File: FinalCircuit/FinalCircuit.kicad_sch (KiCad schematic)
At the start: 59 parts, among them J1 Conn_02x20_Odd_Even, J2 Conn_02x06_Odd_Even, J3 Conn_01x06, U1 LM6172, U10 CD4066BE, U11 CD4066BE, U2 OPA2277, U3 MCP3008, U4 MCP4921, U5 CD4066BE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

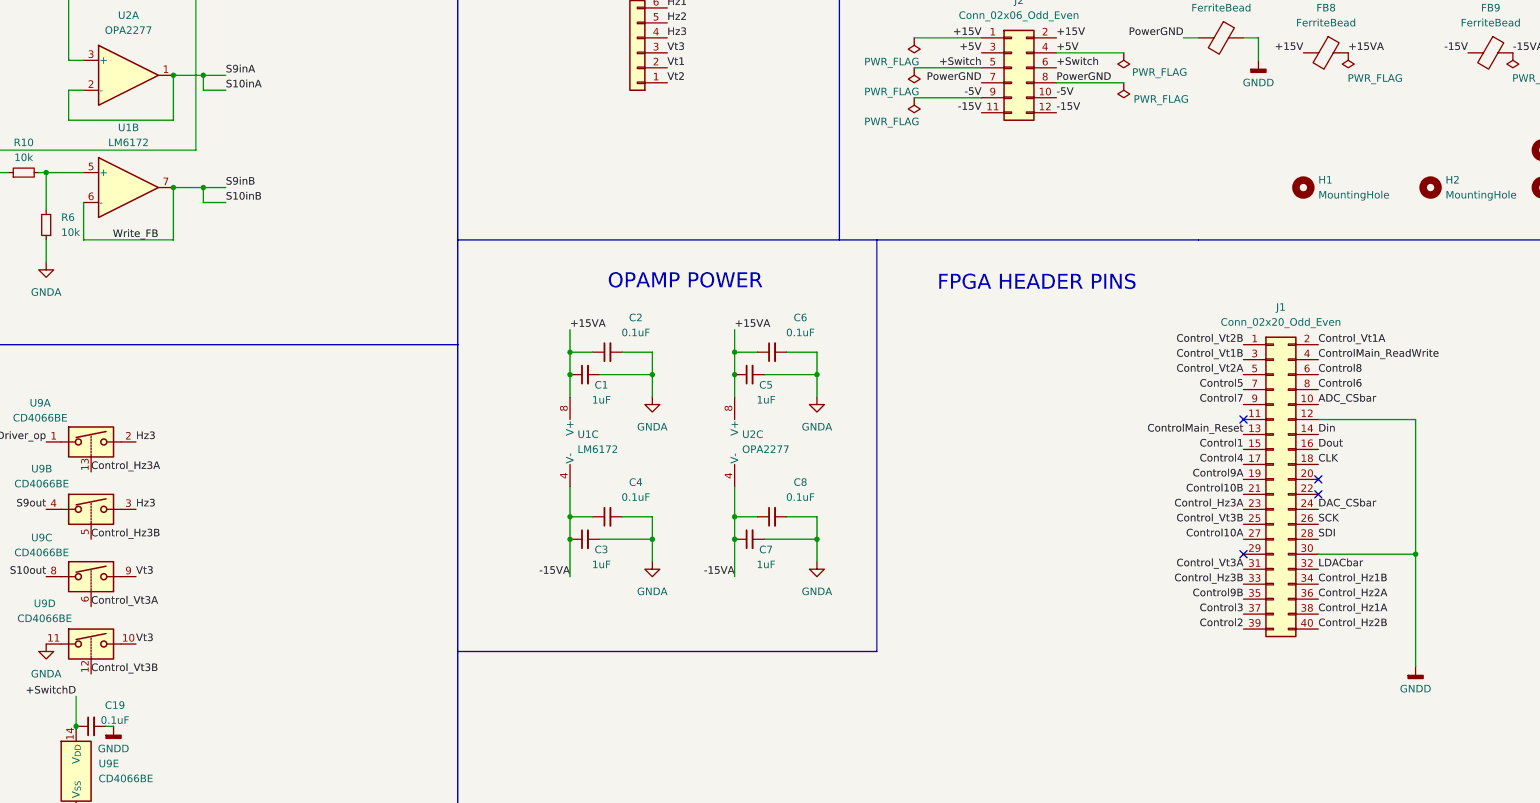
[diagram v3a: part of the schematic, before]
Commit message: Final PCB Done. Resistive Crossbar PCB Done. Verification left.
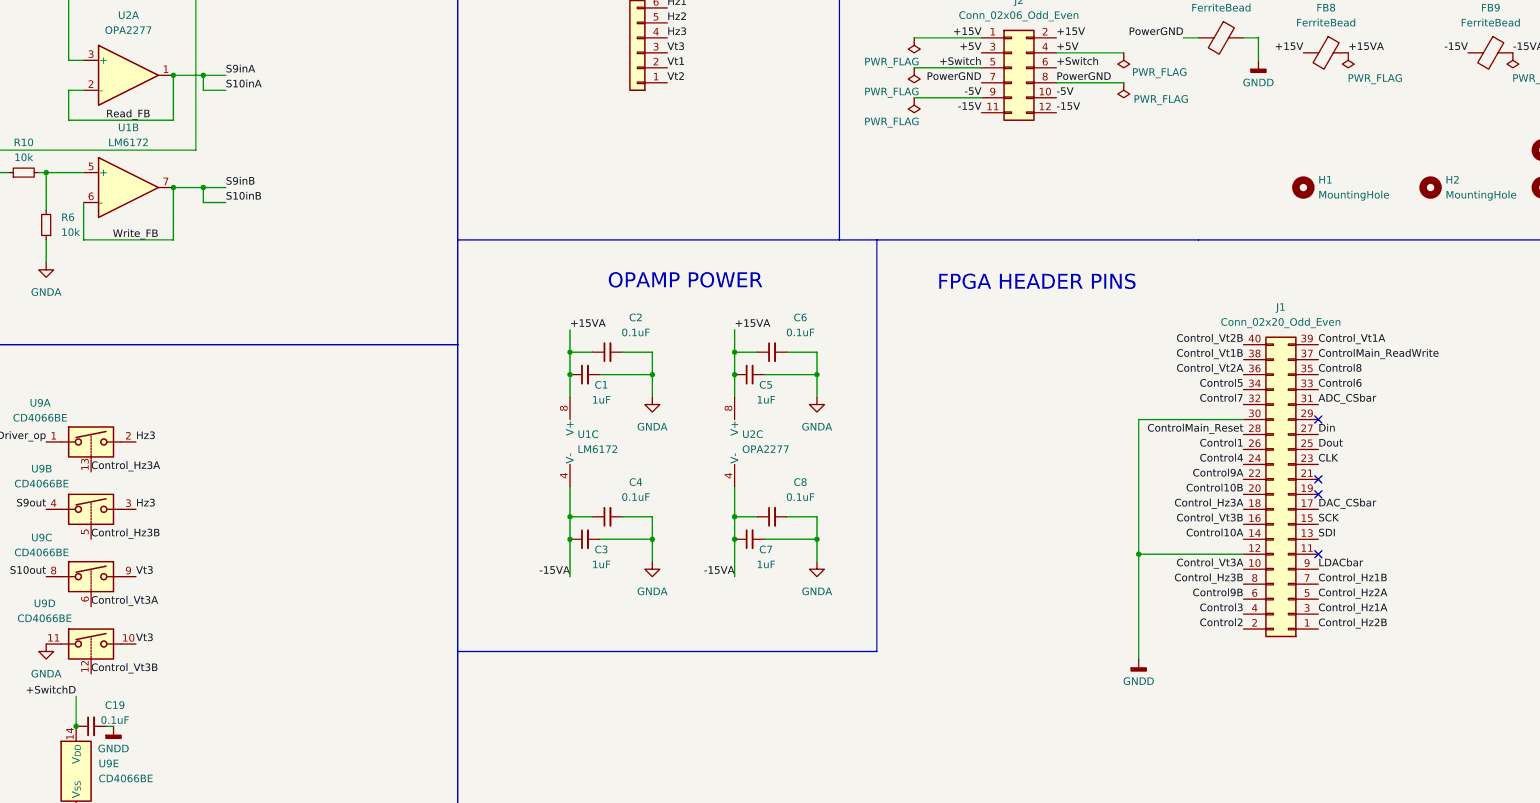
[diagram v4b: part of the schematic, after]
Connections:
- net ADC_CSbar: now also J1.31 (Pin_31); no longer J1.10 (Pin_10)
- net CLK: now also J1.23 (Pin_23); no longer J1.18 (Pin_18)
- net Control1: now also J1.26 (Pin_26); no longer J1.15 (Pin_15)
- net Control10A: now also J1.14 (Pin_14); no longer J1.27 (Pin_27)
- net Control10B: now also J1.20 (Pin_20); no longer J1.21 (Pin_21)
- net Control2: now also J1.2 (Pin_2); no longer J1.39 (Pin_39)
- net Control3: now also J1.4 (Pin_4); no longer J1.37 (Pin_37)
- net Control4: now also J1.24 (Pin_24); no longer J1.17 (Pin_17)
- net Control5: now also J1.34 (Pin_34); no longer J1.7 (Pin_7)
- net Control6: now also J1.33 (Pin_33); no longer J1.8 (Pin_8)
- net Control7: now also J1.32 (Pin_32); no longer J1.9 (Pin_9)
- net Control8: now also J1.35 (Pin_35); no longer J1.6 (Pin_6)
- net Control9A: now also J1.22 (Pin_22); no longer J1.19 (Pin_19)
- net Control9B: now also J1.6 (Pin_6); no longer J1.35 (Pin_35)
- net ControlMain_ReadWrite: now also J1.37 (Pin_37); no longer J1.4 (Pin_4)
- net ControlMain_Reset: now also J1.28 (Pin_28); no longer J1.13 (Pin_13)
- net Control_Hz1A: now also J1.3 (Pin_3); no longer J1.38 (Pin_38)
- net Control_Hz1B: now also J1.7 (Pin_7); no longer J1.34 (Pin_34)
- net Control_Hz2A: now also J1.5 (Pin_5); no longer J1.36 (Pin_36)
- net Control_Hz2B: now also J1.1 (Pin_1); no longer J1.40 (Pin_40)
- net Control_Hz3A: now also J1.18 (Pin_18); no longer J1.23 (Pin_23)
- net Control_Hz3B: now also J1.8 (Pin_8); no longer J1.33 (Pin_33)
- net Control_Vt1A: now also J1.39 (Pin_39); no longer J1.2 (Pin_2)
- net Control_Vt1B: now also J1.38 (Pin_38); no longer J1.3 (Pin_3)
- net Control_Vt2A: now also J1.36 (Pin_36); no longer J1.5 (Pin_5)
- net Control_Vt2B: now also J1.40 (Pin_40); no longer J1.1 (Pin_1)
- net Control_Vt3A: now also J1.10 (Pin_10); no longer J1.31 (Pin_31)
- net Control_Vt3B: now also J1.16 (Pin_16); no longer J1.25 (Pin_25)
- net DAC_CSbar: now also J1.17 (Pin_17); no longer J1.24 (Pin_24)
- net Din: now also J1.27 (Pin_27); no longer J1.14 (Pin_14)
- net Dout: now also J1.25 (Pin_25); no longer J1.16 (Pin_16)
- net LDACbar: now also J1.9 (Pin_9); no longer J1.32 (Pin_32)
- net SCK: now also J1.15 (Pin_15); no longer J1.26 (Pin_26)
- net SDI: now also J1.13 (Pin_13); no longer J1.28 (Pin_28)
- net S10inA renamed Read_FB
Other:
- moved on the sheet: J1
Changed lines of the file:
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@@
 	)
 	(junction
-		(at 361.95 151.13)
-		(diameter 0)
-		(color 0 0 0 0)
-	)
-	(junction
 		(at 114.3 271.78)
 		(diameter 0)
@@
 	)
 	(junction
+		(at 314.96 151.13)
+		(diameter 0)
+		(color 0 0 0 0)
+	)
+	(junction
 		(at 246.38 120.65)
 		(diameter 0)
@@
 	)
 	(no_connect
-		(at 332.74 151.13)
-	)
-	(no_connect
-		(at 332.74 128.27)
-	)
-	(no_connect
 		(at 104.14 257.81)
 	)
@@
 	)
 	(no_connect
+		(at 345.44 128.27)
+	)
+	(no_connect
 		(at 35.56 82.55)
 	)
@@
 	)
 	(no_connect
+		(at 345.44 151.13)
+	)
+	(no_connect
 		(at 88.9 257.81)
 	)
@@
 	(wire
 		(pts
-			(xy 345.44 128.27) (xy 361.95 128.27)
-		)
-		(stroke
-			(width 0)
-			(type default)
-		)
-	)
-	(wire
-		(pts
 			(xy 320.04 45.72) (xy 320.04 49.53)
 		)
@@
 	(wire
 		(pts
+			(xy 314.96 128.27) (xy 314.96 151.13)
+		)
+		(stroke
+			(width 0)
+			(type default)
+		)
+	)
+	(wire
+		(pts
 			(xy 218.44 120.65) (xy 218.44 124.46)
 		)
@@
 	(wire
 		(pts
+			(xy 332.74 128.27) (xy 314.96 128.27)
+		)
+		(stroke
+			(width 0)
+			(type default)
+		)
+	)
+	(wire
+		(pts
 			(xy 96.52 203.2) (xy 96.52 199.39)
 		)
@@
 	(wire
 		(pts
-			(xy 345.44 151.13) (xy 361.95 151.13)
+			(xy 119.38 41.91) (xy 121.92 41.91)
 		)
 		(stroke
@@
 	(wire
 		(pts
-			(xy 119.38 41.91) (xy 121.92 41.91)
+			(xy 260.35 120.65) (xy 260.35 124.46)
 		)
 		(stroke
@@
 	(wire
 		(pts
-			(xy 260.35 120.65) (xy 260.35 124.46)
+			(xy 154.94 54.61) (xy 133.35 54.61)
 		)
 		(stroke
@@
 	(wire
 		(pts
-			(xy 154.94 54.61) (xy 133.35 54.61)
+			(xy 29.21 196.85) (xy 29.21 194.31)
 		)
 		(stroke
@@
 	(wire
 		(pts
-			(xy 29.21 196.85) (xy 29.21 194.31)
+			(xy 314.96 151.13) (xy 332.74 151.13)
 		)
 		(stroke
@@
 	(wire
 		(pts
-			(xy 361.95 151.13) (xy 361.95 170.18)
-		)
-		(stroke
-			(width 0)
-			(type default)
-		)
-	)
-	(wire
-		(pts
 			(xy 116.84 77.47) (xy 116.84 67.31)
 		)
@@
 	(wire
 		(pts
+			(xy 314.96 151.13) (xy 314.96 168.91)
+		)
+		(stroke
+			(width 0)
+			(type default)
+		)
+	)
+	(wire
+		(pts
 			(xy 250.19 116.84) (xy 246.38 116.84)
 		)
@@
 	(wire
 		(pts
-			(xy 361.95 128.27) (xy 361.95 151.13)
-		)
-		(stroke
-			(width 0)
-			(type default)
-		)
-	)
-	(wire
-		(pts
 			(xy 29.21 199.39) (xy 29.21 196.85)
 		)
@@
 		)
 	)
+	(label "Read_FB"
+		(at 139.7 77.47 0)
+		(fields_autoplaced yes)
+		(effects
+			(font
+				(size 1.27 1.27)
+			)
+			(justify left bottom)
+		)
+	)
 	(label "-15VA"
 		(at 218.44 154.94 180)
@@
 	(symbol
 		(lib_id "power:GNDD")
-		(at 361.95 170.18 0)
+		(at 314.96 168.91 0)
 		(unit 1)
 		(exclude_from_sim no)
@@
 		(fields_autoplaced yes)
 		(property "Reference" "#PWR012"
-			(at 361.95 176.53 0)
+			(at 314.96 175.26 0)
 			(effects
 				(font
@@
 		)
 		(property "Value" "GNDD"
-			(at 361.95 173.99 0)
+			(at 314.96 172.72 0)
 			(effects
 				(font
@@
 		)
 		(property "Footprint" ""
-			(at 361.95 170.18 0)
+			(at 314.96 168.91 0)
 			(effects
 				(font
@@
 		)
 		(property "Datasheet" ""
-			(at 361.95 170.18 0)
+			(at 314.96 168.91 0)
 			(effects
 				(font
@@
 		)
 		(property "Description" "Power symbol creates a global label with name \"GNDD\" , digital ground"
-			(at 361.95 170.18 0)
+			(at 314.96 168.91 0)
 			(effects
 				(font
@@
 	(symbol
 		(lib_id "Connector_Generic:Conn_02x20_Odd_Even")
-		(at 337.82 138.43 0)
+		(at 340.36 140.97 180)
 		(unit 1)
 		(exclude_from_sim no)
@@
 		)
 		(property "Footprint" "Connector_PinSocket_2.54mm:PinSocket_2x20_P2.54mm_Vertical"
-			(at 337.82 138.43 0)
+			(at 340.36 140.97 0)
 			(effects
 				(font
@@
 		)
 		(property "Datasheet" "~"
-			(at 337.82 138.43 0)
+			(at 340.36 140.97 0)
 			(effects
 				(font
@@
 		)
 		(property "Description" "Generic connector, double row, 02x20, odd/even pin numbering scheme (row 1 odd numbers, row 2 even numbers), script generated (kicad-library-utils/schlib/autogen/connector/)"
-			(at 337.82 138.43 0)
+			(at 340.36 140.97 0)
 			(effects
 				(font
